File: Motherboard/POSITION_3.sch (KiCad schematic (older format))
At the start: 31 parts, among them Q12 MOSFET_N_(2N7002P,215), Q13 MOSFET_N_(2N7002P,215), Q14 MOSFET_N_(FDMA430NZ), Q15 MOSFET_P_(BS250FTA)

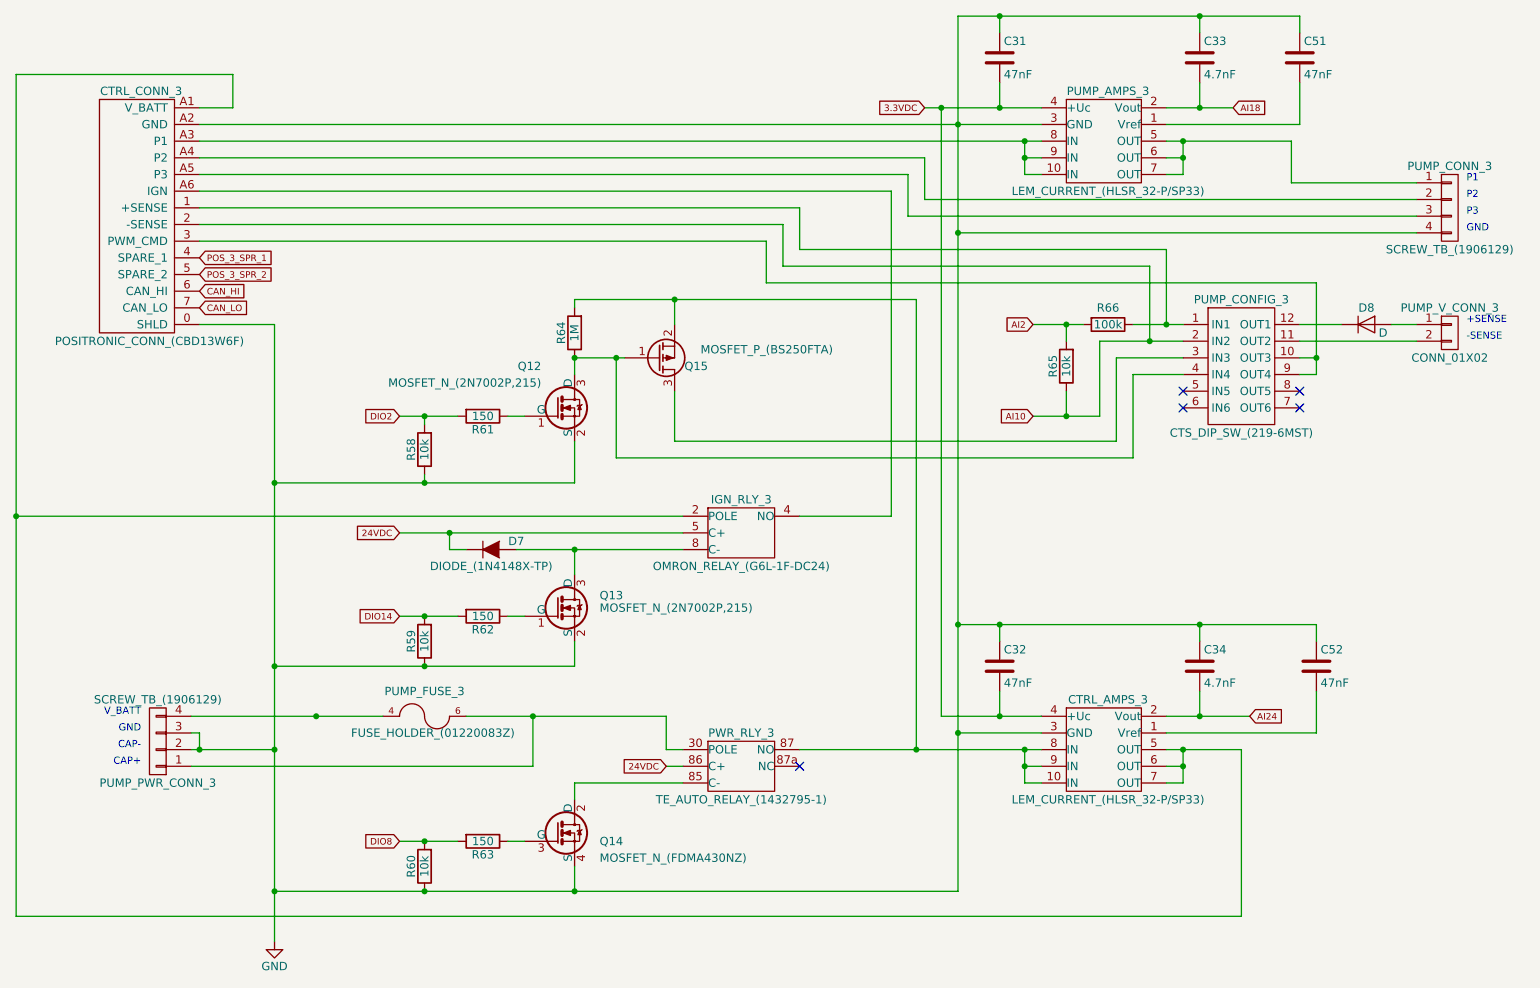
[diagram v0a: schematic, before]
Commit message: - Refer to Google Drive BOM for list of changes for v1.1 - Create drawing for Hella BLDC controller plate.
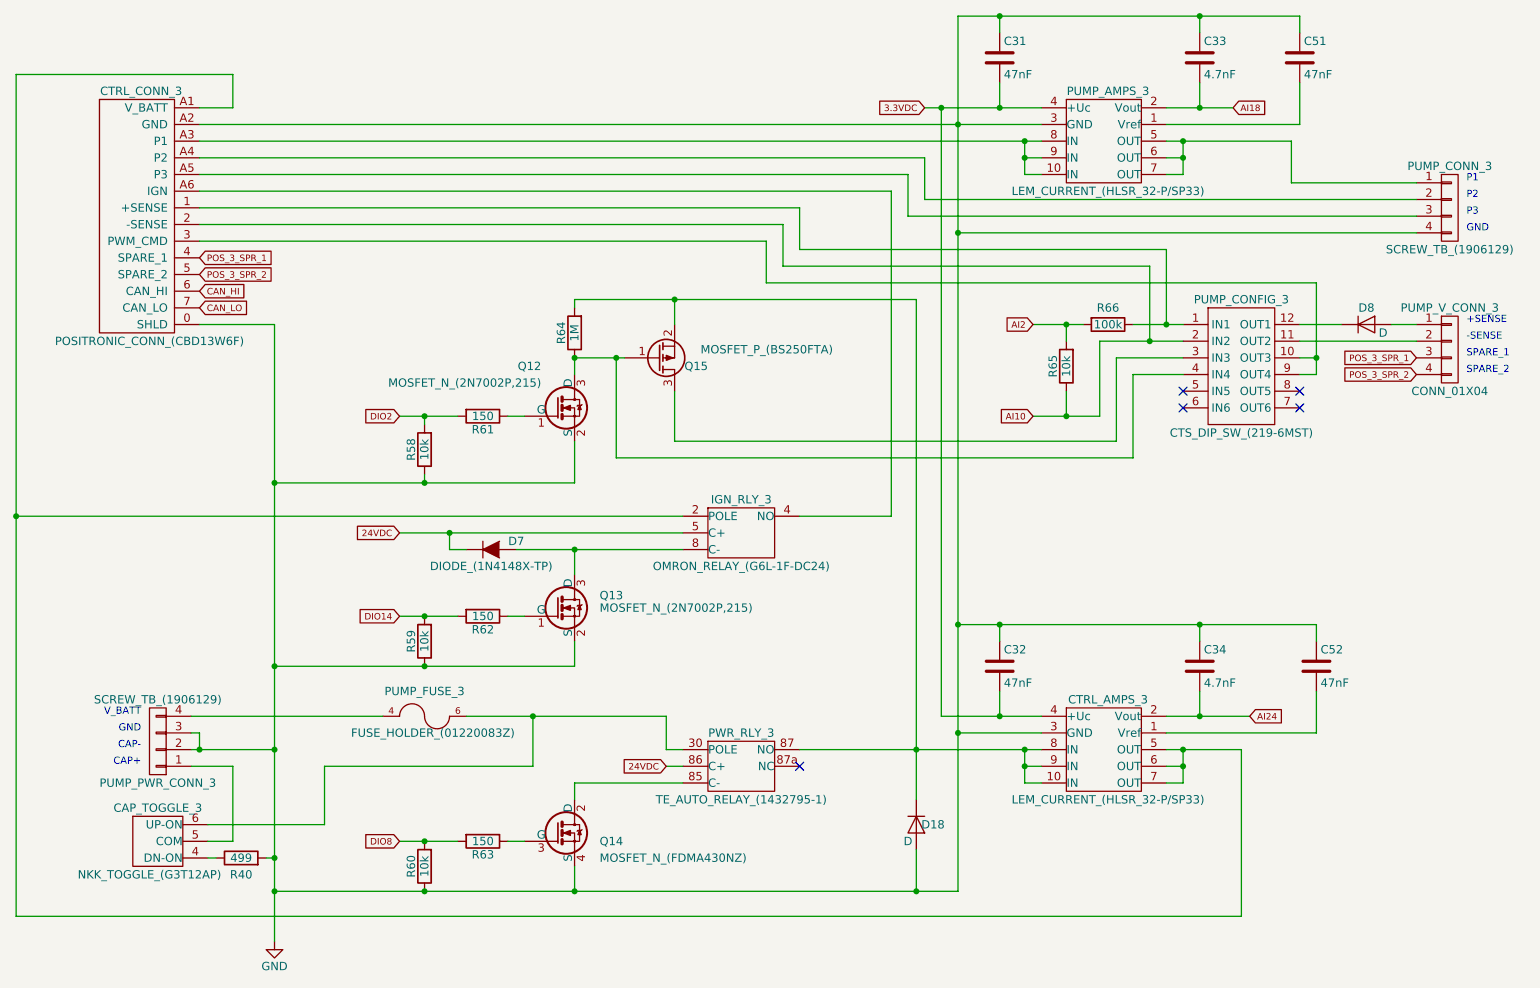
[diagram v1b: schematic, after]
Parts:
- removed PUMP_V_CONN_3: CONN_01X02, Smart_Tank:PHNX_TB_SCREW_2_POS_(1729128), symbol CONN_01X02
- added CAP_TOGGLE_3: NKK_TOGGLE_(G3T12AP), Smart_Tank:NKK_TOGGLE_(G3T12AP), symbol NKK_TOGGLE_(G3T12AP)
- added D18: D, Diodes_SMD:D_SOD-123, symbol D
- added PUMP_V_CONN_3: CONN_01X04, Smart_Tank:PHNX_TB_SCREW_4_POS_(1729144), symbol CONN_01X04
- added R40: 499, Resistors_SMD:R_1206, symbol R
- D8: footprint Diodes_SMD:SOD-523 -> Diodes_SMD:SOD-123
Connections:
- net GND: now also D18.2 (A), R40.2
- net POS_3_SPR_1: now also PUMP_V_CONN_3.3 (P3)
- net POS_3_SPR_2: now also PUMP_V_CONN_3.4 (P4)
- net at PUMP_FUSE_3.6, PUMP_FUSE_3.7, PWR_RLY_3.30 (POLE): now also CAP_TOGGLE_3.6 (UP-ON); no longer PUMP_PWR_CONN_3.1 (P1)
- net at CTRL_AMPS_3.10 (IN), CTRL_AMPS_3.8 (IN), CTRL_AMPS_3.9 (IN)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: now also D18.1 (K)
- net at PUMP_CONFIG_3.11 (OUT2): now also PUMP_V_CONN_3.2 (P2)
- net at D8.2 (A): now also PUMP_V_CONN_3.1 (P1)
- new net: CAP_TOGGLE_3.5 (COM), PUMP_PWR_CONN_3.1 (P1)
- new net: CAP_TOGGLE_3.4 (DN-ON), R40.1
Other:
- note added: "SPARE_1"
- note added: "SPARE_2"
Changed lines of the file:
@@
 CAP+
 $Comp
-L GND #PWR023
+L GND #PWR024
 U 1 1 57A92AD1
 P 3000 6350
-F 0 "#PWR023" H 3000 6100 50  0001 C CNN
+F 0 "#PWR024" H 3000 6100 50  0001 C CNN
 F 1 "GND" H 3000 6200 50  0000 C CNN
 F 2 "" H 3000 6350 50  0000 C CNN
@@
 	1    0    0    -1
 $EndComp
-$Comp
-L CONN_01X02 PUMP_V_CONN_3
-U 1 1 57A92B8D
-P 10050 2700
-F 0 "PUMP_V_CONN_3" H 10050 2850 50  0000 C CNN
-F 1 "CONN_01X02" H 10050 2550 50  0000 C CNN
-F 2 "Smart_Tank:PHNX_TB_SCREW_2_POS_(1729128)" H 10050 2700 50  0001 C CNN
-F 3 "" H 10050 2700 50  0000 C CNN
-	1    10050 2700
-	1    0    0    -1
-$EndComp
 Text Notes 10150 2650 0    43   ~ 0
 +SENSE
@@
 	2550 5100 2550 5200
 Connection ~ 2550 5200
-Wire Wire Line
-	4550 5300 2500 5300
 Connection ~ 4550 5000
 Wire Wire Line
@@
 	4800 2500 6850 2500
 Wire Wire Line
-	6850 2500 6850 5200
+	6850 2500 6850 5500
 Connection ~ 6850 5200
 Wire Wire Line
@@
 	3000 4700 4800 4700
 Connection ~ 3900 4700
-Connection ~ 3250 5000
 Connection ~ 3000 6050
 Wire Wire Line
@@
 F 0 "D8" H 9550 2750 50  0000 C CNN
 F 1 "D" H 9650 2600 50  0000 C CNN
-F 2 "Diodes_SMD:SOD-523" H 9550 2650 50  0001 C CNN
+F 2 "Diodes_SMD:SOD-123" H 9550 2650 50  0001 C CNN
 F 3 "" H 9550 2650 50  0000 C CNN
 	1    9550 2650
@@
 	9250 4450 9250 4550
 Connection ~ 8550 4450
+$Comp
+L NKK_TOGGLE_(G3T12AP) CAP_TOGGLE_3
+U 1 1 59769ABD
+P 2300 5750
+F 0 "CAP_TOGGLE_3" H 2300 5950 50  0000 C CNN
+F 1 "NKK_TOGGLE_(G3T12AP)" H 2250 5550 50  0000 C CNN
+F 2 "Smart_Tank:NKK_TOGGLE_(G3T12AP)" H 2300 4550 50  0001 C CNN
+F 3 "" H 2300 4550 50  0000 C CNN
+	1    2300 5750
+	1    0    0    -1
+$EndComp
+Wire Wire Line
+	2500 5300 2750 5300
+Wire Wire Line
+	2750 5300 2750 5750
+Wire Wire Line
+	3300 5300 4550 5300
+$Comp
+L D D18
+U 1 1 5976AFD3
+P 6850 5650
+F 0 "D18" V 6850 5750 50  0000 C CNN
+F 1 "D" V 6950 5600 50  0000 C CNN
+F 2 "Diodes_SMD:D_SOD-123" H 6850 5650 50  0001 C CNN
+F 3 "" H 6850 5650 50  0000 C CNN
+	1    6850 5650
+	0    1    1    0
+$EndComp
+Wire Wire Line
+	6850 5800 6850 6050
+Connection ~ 6850 6050
+$Comp
+L R R40
+U 1 1 5978C0C0
+P 2800 5850
+F 0 "R40" V 2700 5850 50  0000 C CNN
+F 1 "499" V 2800 5850 50  0000 C CNN
+F 2 "Resistors_SMD:R_1206" V 2730 5850 50  0001 C CNN
+F 3 "" H 2800 5850 50  0000 C CNN
+	1    2800 5850
+	0    -1   -1   0
+$EndComp
+Wire Wire Line
+	2750 5750 2600 5750
+Wire Wire Line
+	2600 5650 3300 5650
+Wire Wire Line
+	3300 5650 3300 5300
+Wire Wire Line
+	2600 5850 2650 5850
+Wire Wire Line
+	2950 5850 3000 5850
+Connection ~ 3000 5850
+$Comp
+L CONN_01X04 PUMP_V_CONN_3
+U 1 1 59799063
+P 10050 2800
+F 0 "PUMP_V_CONN_3" H 10050 3050 50  0000 C CNN
+F 1 "CONN_01X04" H 10050 2550 50  0000 C CNN
+F 2 "Smart_Tank:PHNX_TB_SCREW_4_POS_(1729144)" H 10050 2800 50  0001 C CNN
+F 3 "" H 10050 2800 50  0001 C CNN
+	1    10050 2800
+	1    0    0    -1
+$EndComp
+Text GLabel 9850 2850 0    39   Input ~ 0
+POS_3_SPR_1
+Text GLabel 9850 2950 0    39   Input ~ 0
+POS_3_SPR_2
+Text Notes 10150 2850 0    43   ~ 0
+SPARE_1
+Text Notes 10150 2950 0    43   ~ 0
+SPARE_2
 $EndSCHEMATC

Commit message: - Created Modbus Adapter.
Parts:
- C31, C32, C33, C34, C51, C52: symbol C -> Smart-Tank-Motherboard-rescue:C
- CAP_TOGGLE_3: symbol NKK_TOGGLE_(G3T12AP) -> Smart-Tank-Motherboard-rescue:NKK_TOGGLE_(G3T12AP)
- CTRL_AMPS_3, PUMP_AMPS_3: symbol LEM_CURRENT_(HLSR_32-P/SP33) -> Smart-Tank-Motherboard-rescue:LEM_CURRENT_(HLSR_32-P_SP33)
- CTRL_CONN_3: symbol POSITRONIC_CONN_(CBD13W6F) -> Smart-Tank-Motherboard-rescue:POSITRONIC_CONN_(CBD13W6F)
- D18, D8: symbol D -> Smart-Tank-Motherboard-rescue:D
- D7: symbol DIODE_(1N4148X-TP) -> Smart-Tank-Motherboard-rescue:DIODE_(1N4148X-TP)
- IGN_RLY_3: symbol OMRON_RELAY_(G6L-1F-DC24) -> Smart-Tank-Motherboard-rescue:OMRON_RELAY_(G6L-1F-DC24)
- PUMP_CONFIG_3: symbol CTS_DIP_SW_(219-6MST) -> Smart-Tank-Motherboard-rescue:CTS_DIP_SW_(219-6MST)
- PUMP_CONN_3, PUMP_PWR_CONN_3: symbol SCREW_TB_(1906129) -> Smart-Tank-Motherboard-rescue:SCREW_TB_(1906129)
- PUMP_FUSE_3: symbol FUSE_HOLDER_(01220083Z) -> Smart-Tank-Motherboard-rescue:FUSE_HOLDER_(01220083Z)
- PUMP_V_CONN_3: symbol CONN_01X04 -> Smart-Tank-Motherboard-rescue:CONN_01X04
- PWR_RLY_3: symbol TE_AUTO_RELAY_(1432795-1) -> Smart-Tank-Motherboard-rescue:TE_AUTO_RELAY_(1432795-1)
- Q12, Q13: symbol MOSFET_N_(2N7002P,215) -> Smart-Tank-Motherboard-rescue:MOSFET_N_(2N7002P,215)
- Q14: symbol MOSFET_N_(FDMA430NZ) -> Smart-Tank-Motherboard-rescue:MOSFET_N_(FDMA430NZ)
- Q15: symbol MOSFET_P_(BS250FTA) -> Smart-Tank-Motherboard-rescue:MOSFET_P_(BS250FTA)
- R40, R58, R59, R60, R61, R62, R63, R64, R65, R66: symbol R -> Smart-Tank-Motherboard-rescue:R
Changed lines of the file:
@@
-EESchema Schematic File Version 2
-LIBS:Smart Tank Motherboard-rescue
-LIBS:power
-LIBS:device
-LIBS:transistors
-LIBS:conn
-LIBS:linear
-LIBS:regul
-LIBS:74xx
-LIBS:cmos4000
-LIBS:adc-dac
-LIBS:memory
-LIBS:xilinx
-LIBS:microcontrollers
-LIBS:dsp
-LIBS:microchip
-LIBS:analog_switches
-LIBS:motorola
-LIBS:texas
-LIBS:intel
-LIBS:audio
-LIBS:interface
-LIBS:digital-audio
-LIBS:philips
-LIBS:display
-LIBS:cypress
-LIBS:siliconi
-LIBS:opto
-LIBS:atmel
-LIBS:contrib
-LIBS:valves
+EESchema Schematic File Version 4
 LIBS:Smart Tank Motherboard-cache
-EELAYER 25 0
+EELAYER 29 0
 EELAYER END
 $Descr A4 11693 8268
@@
 $EndDescr
 $Comp
-L R R63
+L Smart-Tank-Motherboard-rescue:R R63
 U 1 1 57A92AB7
 P 4250 5750
@@
 $EndComp
 $Comp
-L R R60
+L Smart-Tank-Motherboard-rescue:R R60
 U 1 1 57A92ABE
 P 3900 5900
@@
 $EndComp
 $Comp
-L SCREW_TB_(1906129) PUMP_PWR_CONN_3
+L Smart-Tank-Motherboard-rescue:SCREW_TB_(1906129) PUMP_PWR_CONN_3
 U 1 1 57A92AC6
 P 2300 5150
@@
 CAP+
 $Comp
-L GND #PWR024
+L Smart-Tank-Motherboard-rescue:GND #PWR024
 U 1 1 57A92AD1
 P 3000 6350
@@
 $EndComp
 $Comp
-L SCREW_TB_(1906129) PUMP_CONN_3
+L Smart-Tank-Motherboard-rescue:SCREW_TB_(1906129) PUMP_CONN_3
 U 1 1 57A92AE6
 P 10050 1950
@@
 GND
 $Comp
-L POSITRONIC_CONN_(CBD13W6F) CTRL_CONN_3
+L Smart-Tank-Motherboard-rescue:POSITRONIC_CONN_(CBD13W6F) CTRL_CONN_3
 U 1 1 57A92AF1
 P 2200 1900
@@
 $EndComp
 $Comp
-L FUSE_HOLDER_(01220083Z) PUMP_FUSE_3
+L Smart-Tank-Motherboard-rescue:FUSE_HOLDER_(01220083Z) PUMP_FUSE_3
 U 1 1 57A92AF8
 P 3900 5000
@@
 $EndComp
 $Comp
-L MOSFET_N_(FDMA430NZ) Q14
+L Smart-Tank-Motherboard-rescue:MOSFET_N_(FDMA430NZ) Q14
 U 1 1 57A92AFF
 P 4700 5700
@@
 $EndComp
 $Comp
-L TE_AUTO_RELAY_(1432795-1) PWR_RLY_3
+L Smart-Tank-Motherboard-rescue:TE_AUTO_RELAY_(1432795-1) PWR_RLY_3
 U 1 1 57A92B06
 P 5700 5400
@@
 AI24
 $Comp
-L OMRON_RELAY_(G6L-1F-DC24) IGN_RLY_3
+L Smart-Tank-Motherboard-rescue:OMRON_RELAY_(G6L-1F-DC24) IGN_RLY_3
 U 1 1 57A92B12
 P 5700 4000
@@
 $EndComp
 $Comp
-L MOSFET_N_(2N7002P,215) Q13
+L Smart-Tank-Motherboard-rescue:MOSFET_N_(2N7002P,215) Q13
 U 1 1 57A92B19
 P 4700 4350
@@
 $EndComp
 $Comp
-L R R62
+L Smart-Tank-Motherboard-rescue:R R62
 U 1 1 57A92B20
 P 4250 4400
@@
 $EndComp
 $Comp
-L R R59
+L Smart-Tank-Motherboard-rescue:R R59
 U 1 1 57A92B27
 P 3900 4550
@@
 CAN_LO
 $Comp
-L DIODE_(1N4148X-TP) D7
+L Smart-Tank-Motherboard-rescue:DIODE_(1N4148X-TP) D7
 U 1 1 57A92B32
 P 4300 4000
@@
 POS_3_SPR_2
 $Comp
-L MOSFET_N_(2N7002P,215) Q12
+L Smart-Tank-Motherboard-rescue:MOSFET_N_(2N7002P,215) Q12
 U 1 1 57A92B3B
 P 4700 3150
@@
 $EndComp
 $Comp
-L MOSFET_P_(BS250FTA) Q15
+L Smart-Tank-Motherboard-rescue:MOSFET_P_(BS250FTA) Q15
 U 1 1 57A92B42
 P 5300 2850
@@
 $EndComp
 $Comp
-L R R61
+L Smart-Tank-Motherboard-rescue:R R61
 U 1 1 57A92B49
 P 4250 3200
@@
 $EndComp
 $Comp
-L R R64
+L Smart-Tank-Motherboard-rescue:R R64
 U 1 1 57A92B50
 P 4800 2700
@@
 DIO2
 $Comp
-L R R58
+L Smart-Tank-Motherboard-rescue:R R58
 U 1 1 57A92B58
 P 3900 3400
@@
 NoConn ~ 6150 5300
 $Comp
-L C C33
+L Smart-Tank-Motherboard-rescue:C C33
 U 1 1 57A92B6A
 P 8550 1050
@@
 $EndComp
 $Comp
-L C C31
+L Smart-Tank-Motherboard-rescue:C C31
 U 1 1 57A92B71
 P 7350 1050
@@
 $EndComp
 $Comp
-L C C34
+L Smart-Tank-Motherboard-rescue:C C34
 U 1 1 57A92B78
 P 8550 4700
@@
 $EndComp
 $Comp
-L C C32
+L Smart-Tank-Motherboard-rescue:C C32
 U 1 1 57A92B7F
 P 7350 4700
@@
 $EndComp
 $Comp
-L CTS_DIP_SW_(219-6MST) PUMP_CONFIG_3
+L Smart-Tank-Motherboard-rescue:CTS_DIP_SW_(219-6MST) PUMP_CONFIG_3
 U 1 1 57A92B86
 P 8800 2900
@@
 NoConn ~ 8450 3150
 $Comp
-L R R65
+L Smart-Tank-Motherboard-rescue:R R65
 U 1 1 57A92B9A
 P 7750 2900
@@
 $EndComp
 $Comp
-L R R66
+L Smart-Tank-Motherboard-rescue:R R66
 U 1 1 57A92BA1
 P 8000 2650
@@
 	4800 2550 4800 2500
 $Comp
-L D D8
+L Smart-Tank-Motherboard-rescue:D D8
 U 1 1 57A92C5F
 P 9550 2650
@@
 	9700 2650 9850 2650
 $Comp
-L LEM_CURRENT_(HLSR_32-P/SP33) PUMP_AMPS_3
+L Smart-Tank-Motherboard-rescue:LEM_CURRENT_(HLSR_32-P_SP33) PUMP_AMPS_3
 U 1 1 57B744CA
 P 7850 1550
@@
 $EndComp
 $Comp
-L LEM_CURRENT_(HLSR_32-P/SP33) CTRL_AMPS_3
+L Smart-Tank-Motherboard-rescue:LEM_CURRENT_(HLSR_32-P_SP33) CTRL_AMPS_3
 U 1 1 57B76519
 P 7850 5200
@@
 Connection ~ 3000 3600
 $Comp
-L C C51
+L Smart-Tank-Motherboard-rescue:C C51
 U 1 1 57D1E7D7
 P 9150 1050
@@
 Connection ~ 8550 800
 $Comp
-L C C52
+L Smart-Tank-Motherboard-rescue:C C52
 U 1 1 57D1EEF9
 P 9250 4700
@@
 Connection ~ 8550 4450
 $Comp
-L NKK_TOGGLE_(G3T12AP) CAP_TOGGLE_3
+L Smart-Tank-Motherboard-rescue:NKK_TOGGLE_(G3T12AP) CAP_TOGGLE_3
 U 1 1 59769ABD
 P 2300 5750
@@
 	3300 5300 4550 5300
 $Comp
-L D D18
+L Smart-Tank-Motherboard-rescue:D D18
 U 1 1 5976AFD3
 P 6850 5650
@@
 Connection ~ 6850 6050
 $Comp
-L R R40
+L Smart-Tank-Motherboard-rescue:R R40
 U 1 1 5978C0C0
 P 2800 5850
@@
 Connection ~ 3000 5850
 $Comp
-L CONN_01X04 PUMP_V_CONN_3
+L Smart-Tank-Motherboard-rescue:CONN_01X04 PUMP_V_CONN_3
 U 1 1 59799063
 P 10050 2800
